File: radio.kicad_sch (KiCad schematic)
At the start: 0 parts

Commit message: Added some components
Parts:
- added U501: nRF24L01P, Package_DFN_QFN:QFN-20-1EP_4x4mm_P0.5mm_EP2.5x2.5mm, symbol RF:nRF24L01P
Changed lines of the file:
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@@
 (kicad_sch (version 20230121) (generator eeschema)
   (paper "A4")
+  (symbol (lib_id "RF:nRF24L01P") (at 127.635 95.885 0) (unit 1)
+    (in_bom yes) (on_board yes) (dnp no) (fields_autoplaced)
+    (property "Reference" "U501" (at 132.3691 74.93 0)
+      (effects (font (size 1.27 1.27)) (justify left))
+    )
+    (property "Value" "nRF24L01P" (at 132.3691 77.47 0)
+      (effects (font (size 1.27 1.27)) (justify left))
+    )
+    (property "Footprint" "Package_DFN_QFN:QFN-20-1EP_4x4mm_P0.5mm_EP2.5x2.5mm" (at 132.715 75.565 0)
+      (effects (font (size 1.27 1.27) italic) (justify left) hide)
+    )
+    (property "Datasheet" "http://www.nordicsemi.com/eng/content/download/2726/34069/file/nRF24L01P_Product_Specification_1_0.pdf" (at 127.635 93.345 0)
+      (effects (font (size 1.27 1.27)) hide)
+    )
+    (pin "1")
+    (pin "10")
+    (pin "11")
+    (pin "12")
+    (pin "13")
+    (pin "14")
+    (pin "15")
+    (pin "16")
+    (pin "17")
+    (pin "18")
+    (pin "19")
+    (pin "2")
+    (pin "20")
+    (pin "3")
+    (pin "4")
+    (pin "5")
+    (pin "6")
+    (pin "7")
+    (pin "8")
+    (pin "9")
+    (instances
+      (project "MicroQuad"
+        (path "/8971f876-5b3c-4165-aa17-84d4a3cd004e/b8de5233-e42e-4694-ac5f-248bc2666d9d"
+          (reference "U501") (unit 1)
+        )
+      )
+    )
+  )
 )

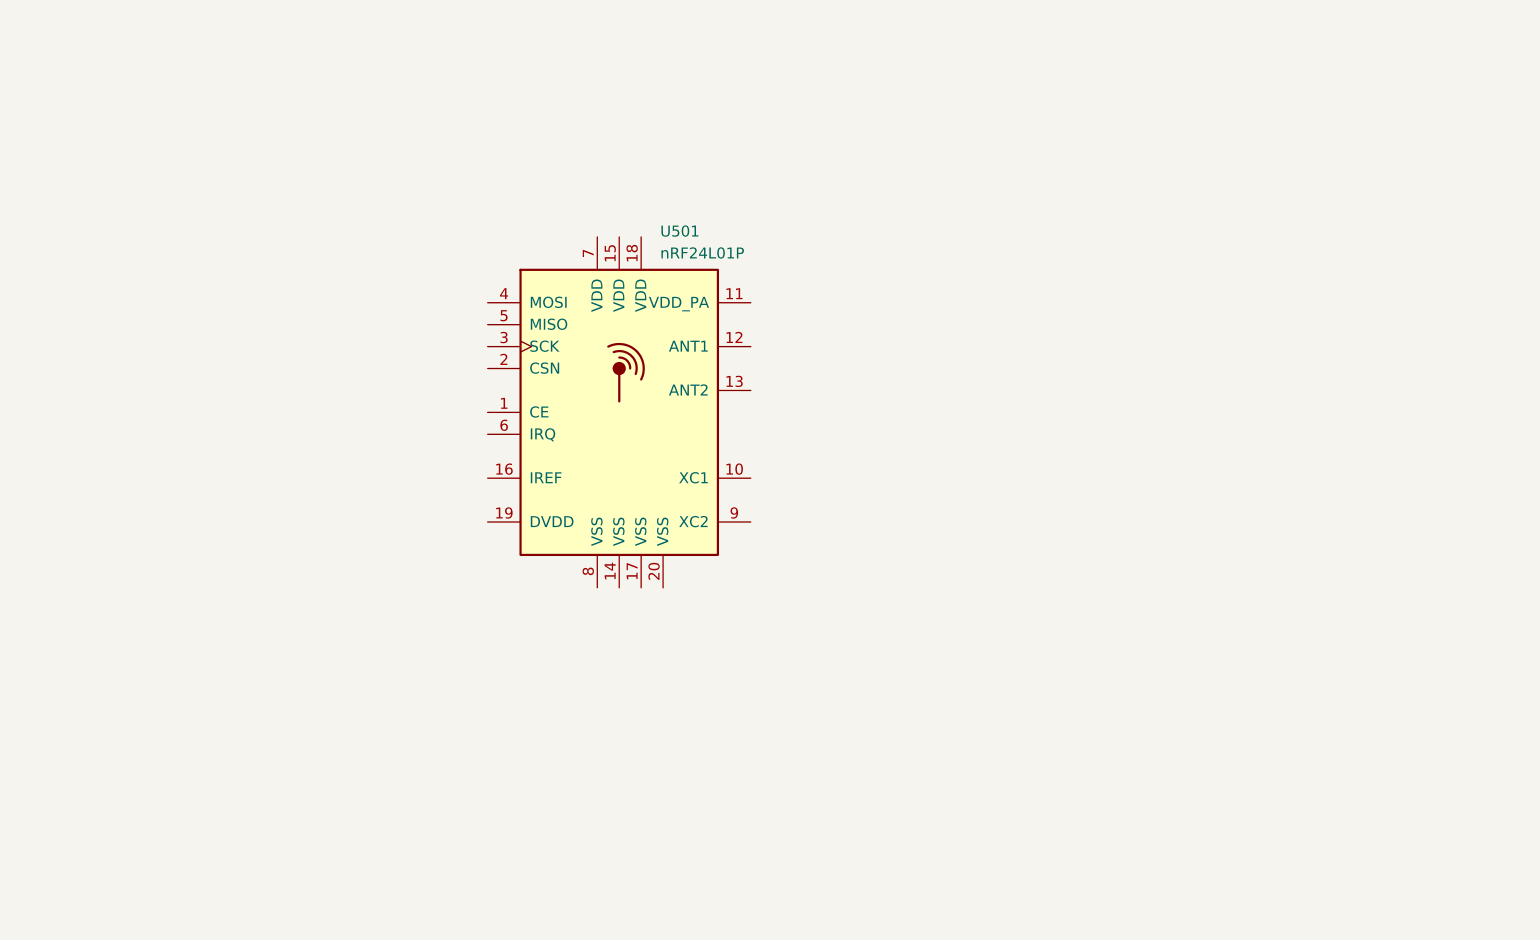
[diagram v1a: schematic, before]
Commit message: Added crystal and matching network for nrf24
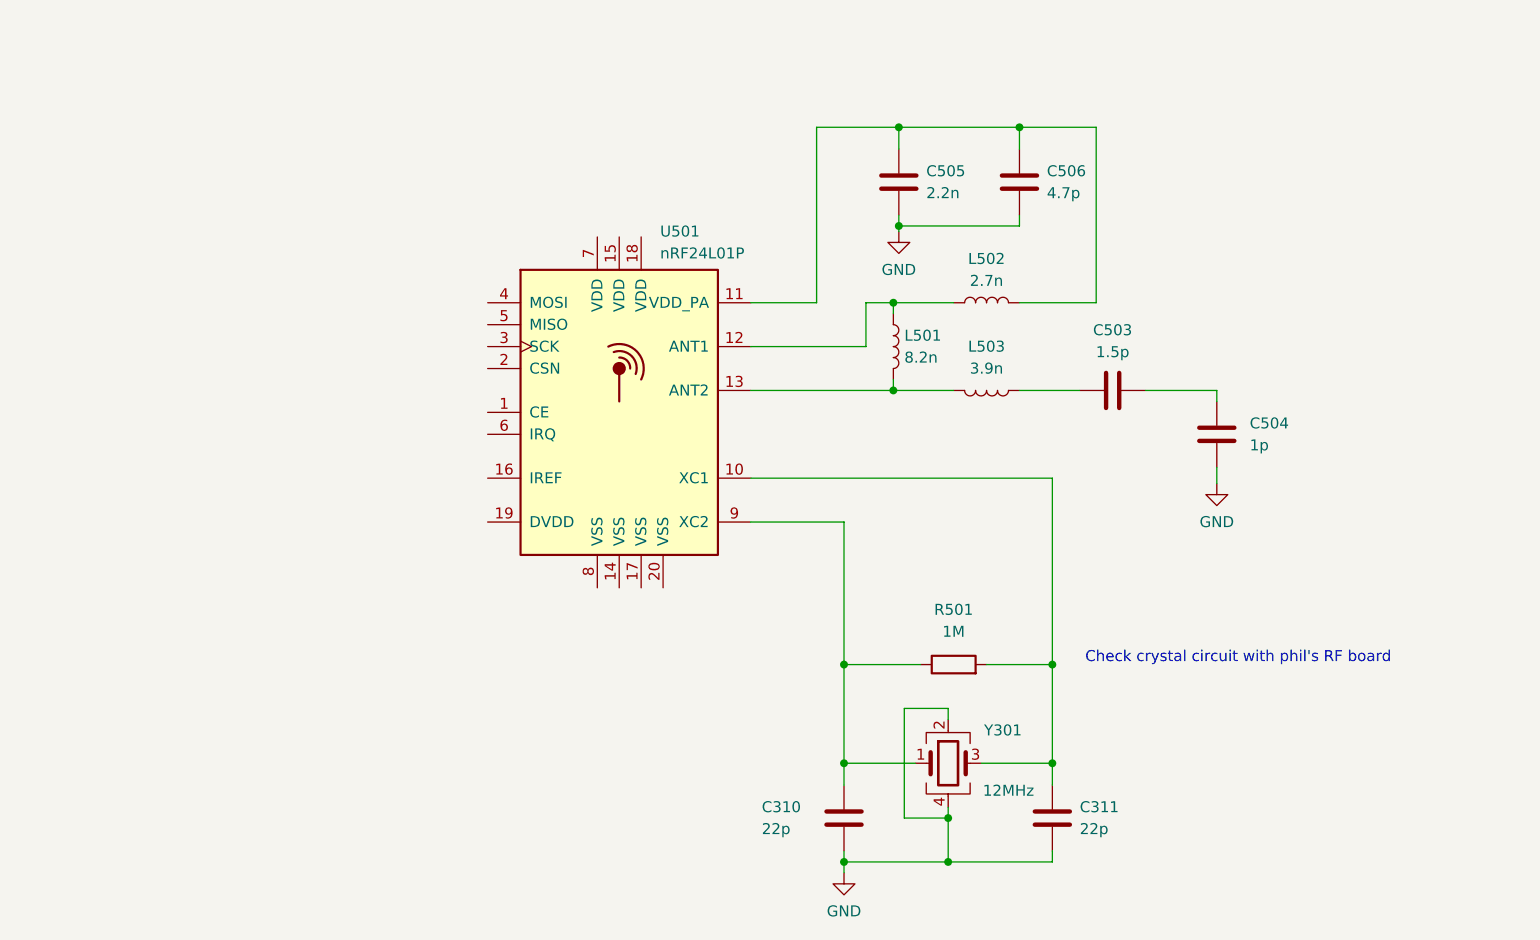
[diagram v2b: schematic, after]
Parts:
- added C310, C311: 22p, symbol Device:C
- added C503: 1.5p, symbol Device:C
- added C504: 1p, symbol Device:C
- added C505: 2.2n, symbol Device:C
- added C506: 4.7p, symbol Device:C
- added L501: 8.2n, symbol Device:L
- added L502: 2.7n, symbol Device:L
- added L503: 3.9n, symbol Device:L
- added R501: 1M, symbol Device:R
- added Y301: 12MHz, symbol Device:Crystal_GND24
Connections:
- net at U501.10 (XC1): now also C311.1, R501.2, Y301.3
- net at U501.11 (VDD_PA): now also C505.1, C506.1, L502.2
- net at U501.12 (ANT1): now also L501.1, L502.1
- net at U501.13 (ANT2): now also L501.2, L503.2
- net at U501.9 (XC2): now also C310.1, R501.1, Y301.1
- new net: C503.1, L503.1
- new net: C503.2, C504.2
- new net GND: C310.2, C311.2, C504.1, C505.2, C506.2, Y301.2, Y301.4
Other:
- note added: "Check crystal circuit with phil's RF board"

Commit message: Finished connections for nrf24
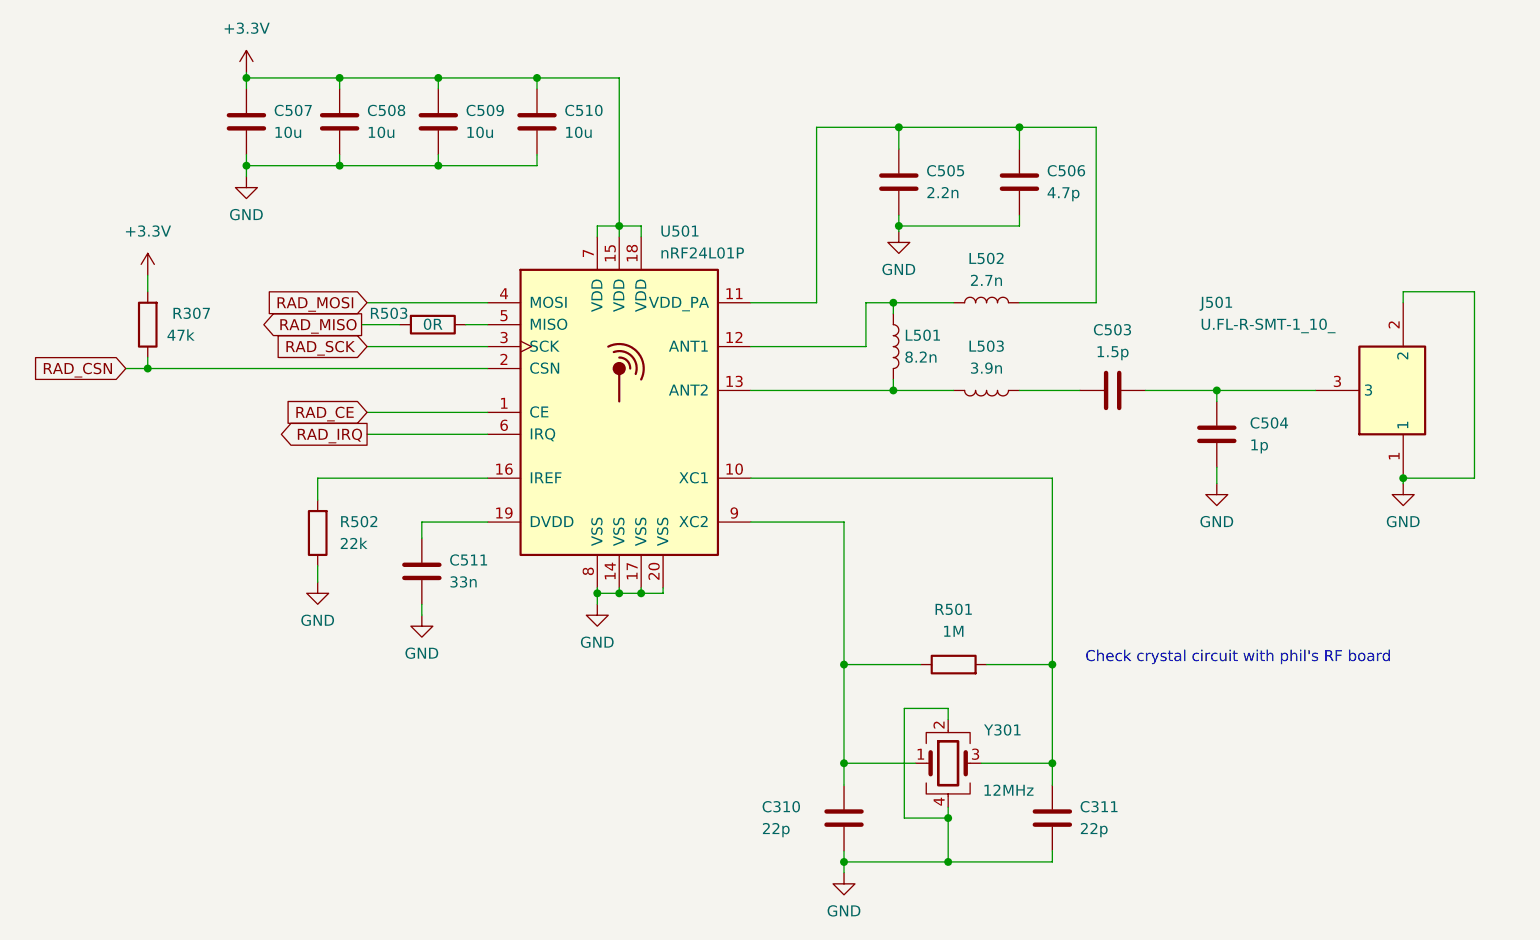
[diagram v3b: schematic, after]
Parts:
- added C507, C508, C509, C510: 10u, symbol Device:C
- added C511: 33n, symbol Device:C
- added J501: U.FL-R-SMT-1_10_, U.FL-R-SMT-1(10), symbol U_FL-R-SMT-1_10_:U.FL-R-SMT-1_10_
- added R307: 47k, symbol Device:R
- added R502: 22k, symbol Device:R
- added R503: 0R, symbol Device:R
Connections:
- net GND: now also U501.14 (VSS), U501.17 (VSS), U501.20 (VSS), U501.8 (VSS), C507.2, C508.2, C509.2, C510.2, C511.2, J501.1, J501.2, R502.1
- net RAD_CE: now reaches U501.1 (CE)
- net +3.3V: now reaches U501.15 (VDD)
- net +3.3V: now also U501.18 (VDD), U501.7 (VDD), C507.1, C508.1, C509.1, C510.1, R307.2
- net at U501.16 (IREF): now also R502.2
- net at U501.19 (DVDD): now also C511.1
- net RAD_CSN: now reaches U501.2 (CSN)
- net RAD_CSN: now also R307.1
- net RAD_SCK: now reaches U501.3 (SCK)
- net RAD_MOSI: now reaches U501.4 (MOSI)
- net at U501.5 (MISO): now also R503.1
- net RAD_IRQ: now reaches U501.6 (IRQ)
- net at C503.2, C504.2: now also J501.3
- new net RAD_MISO: R503.2
